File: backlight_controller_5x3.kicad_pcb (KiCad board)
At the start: 2 copper layers, 121.3 x 67.3 mm, 39 parts, among them J1 M12-5_RCPT_F, J2 M12-5_RCPT_F, J3 DB9F, J4 DB9M, P1 MINI_FIT_JR_02X03_M_RA, P2 PWR_JACK_2.5x5.5, U1 SN74ABT541BDWR, U2 SN74ABT541BDWR

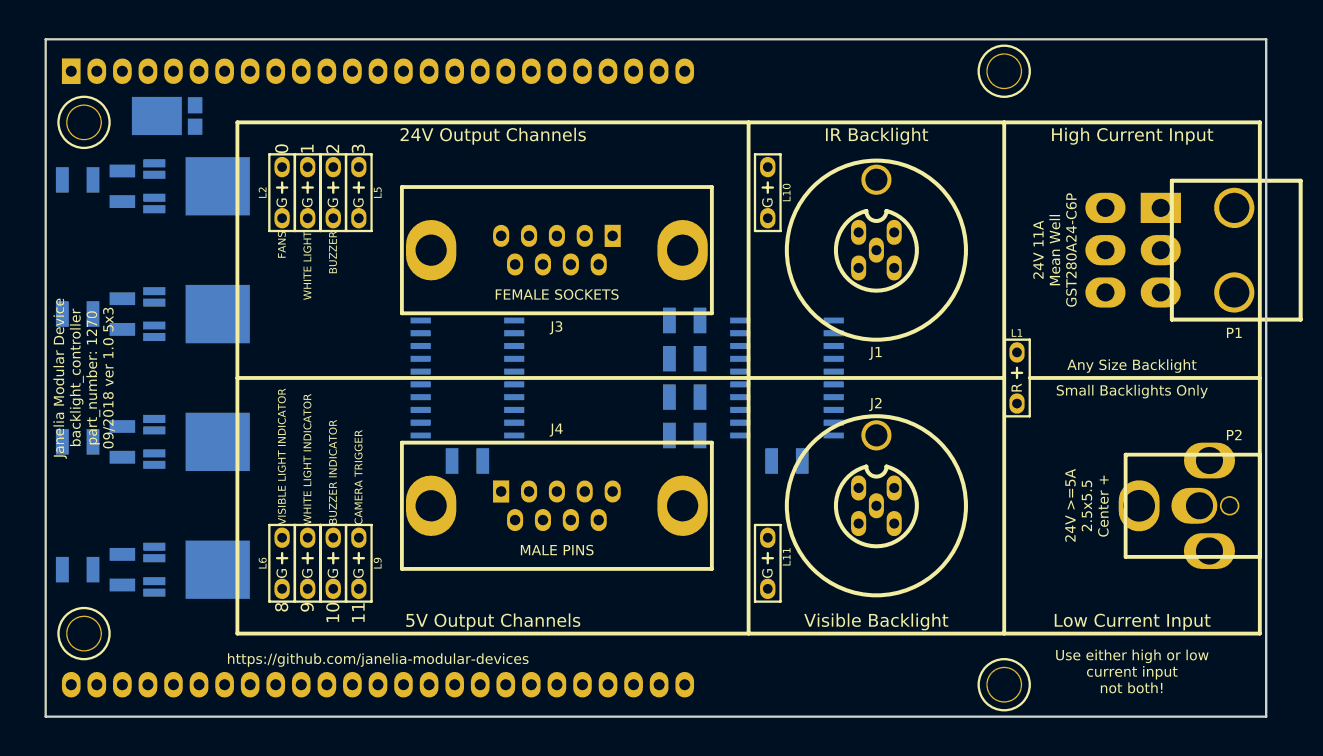
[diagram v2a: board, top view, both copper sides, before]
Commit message: Initial footprint layout.
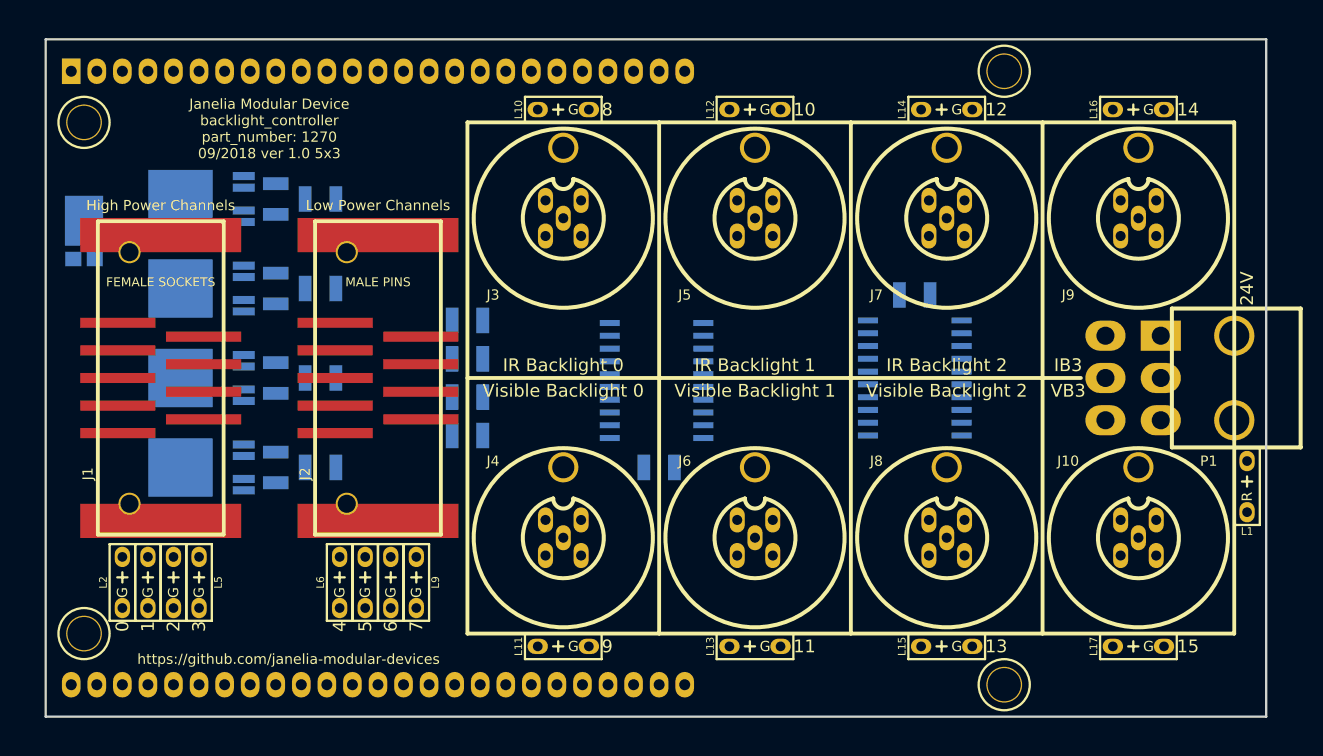
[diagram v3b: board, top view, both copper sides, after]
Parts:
- removed P2: PWR_JACK_2.5x5.5, backlight_controller_5x3:DCJACK_2PIN_HIGHCURRENT
- added J10: M12-5_RCPT_F, backlight_controller_5x3:M12-5_RCPT_F, F.Cu at (178.4, 121.3)
- added J5: M12-5_RCPT_F, backlight_controller_5x3:M12-5_RCPT_F, F.Cu at (140.3, 89.5)
- added J6: M12-5_RCPT_F, backlight_controller_5x3:M12-5_RCPT_F, F.Cu at (140.3, 121.3)
- added J7: M12-5_RCPT_F, backlight_controller_5x3:M12-5_RCPT_F, F.Cu at (159.4, 89.5)
- added J8: M12-5_RCPT_F, backlight_controller_5x3:M12-5_RCPT_F, F.Cu at (159.4, 121.3)
- added J9: M12-5_RCPT_F, backlight_controller_5x3:M12-5_RCPT_F, F.Cu at (178.4, 89.5)
- added L12: LED_5V_GRN, backlight_controller_5x3:LED_555-3XXX_G, F.Cu at (140.3, 78.7)
- added L13: LED_5V_GRN, backlight_controller_5x3:LED_555-3XXX_G, F.Cu at (140.3, 132.1)
- added L14: LED_5V_GRN, backlight_controller_5x3:LED_555-3XXX_G, F.Cu at (159.4, 78.7)
- added L15: LED_5V_GRN, backlight_controller_5x3:LED_555-3XXX_G, F.Cu at (159.4, 132.1)
- added L16: LED_5V_GRN, backlight_controller_5x3:LED_555-3XXX_G, F.Cu at (178.4, 78.7)
- added L17: LED_5V_GRN, backlight_controller_5x3:LED_555-3XXX_G, F.Cu at (178.4, 132.1)
- J1: value M12-5_RCPT_F -> DB9F_SMD; footprint backlight_controller_5x3:M12-5_RCPT_F -> footprints:DB9F_SMD
- J2: value M12-5_RCPT_F -> DB9M_SMD; footprint backlight_controller_5x3:M12-5_RCPT_F -> footprints:DB9M_SMD
- J3: value DB9F -> M12-5_RCPT_F; footprint backlight_controller_5x3:DB9F -> backlight_controller_5x3:M12-5_RCPT_F
- J4: value DB9M -> M12-5_RCPT_F; footprint backlight_controller_5x3:DB9M -> backlight_controller_5x3:M12-5_RCPT_F
- R5, R6, R7, R8: value 35.7 -> 140
- moved J1 72.2 mm to (81.3, 105.4), turned to 90 degrees
- moved J2 51.1 mm to (102.9, 105.4), turned to 90 degrees
- moved L2 41.9 mm to (77.5, 125.7)
- moved L3 41.9 mm to (80.0, 125.7)
- moved L4 41.9 mm to (82.5, 125.7)
- moved L5 41.9 mm to (85.1, 125.7)
- moved R4 26.2 mm to (97.2, 114.3), turned to 0 degrees
- moved L1 25.3 mm to (189.2, 116.2)
- moved R3 25.0 mm to (97.2, 105.4), turned to 0 degrees
- moved R2 24.3 mm to (97.2, 96.5), turned to 0 degrees
- moved R1 24.2 mm to (97.2, 87.6), turned to 0 degrees
- moved L10 21.9 mm to (121.3, 78.7), turned to 90 degrees
- moved L11 21.9 mm to (121.3, 132.1), turned to 90 degrees
- moved R5 21.6 mm to (111.8, 99.7)
- moved R6 21.6 mm to (111.8, 103.5)
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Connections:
- net /output_0/FAULT renamed /high_power_outputs/fans/FAULT
- net /output_1/FAULT renamed /high_power_outputs/white_light/FAULT
- net /output_2/FAULT renamed /high_power_outputs/buzzer/FAULT
- net /output_3/FAULT renamed /high_power_outputs/output_3/FAULT
- HPS1 pad 6: /FANS -> /high_power_outputs/OUTPUT_0
- HPS2 pad 6: /WHITE_LIGHT -> /high_power_outputs/OUTPUT_1
- HPS3 pad 6: /BUZZER -> /high_power_outputs/OUTPUT_2
- HPS4 pad 6: /OUTPUT_3 -> /high_power_outputs/OUTPUT_3
- J1 pad 2: (no net) -> /high_power_outputs/OUTPUT_0
- J1 pad 3: GND -> VAA
- J1 pad 4: /C_12 -> /high_power_outputs/OUTPUT_1
- J2 pad 1: VAA -> GND
- J2 pad 2: (no net) -> /low_power_outputs/OUTPUT_0
- J2 pad 4: /C_13 -> /low_power_outputs/OUTPUT_1
- J2 pad 5: VAA -> GND
- J3 pad 2: /FANS -> (no net)
- J3 pad 3: VAA -> GND
- J3 pad 4: /WHITE_LIGHT -> /C_8
- J4 pad 1: GND -> VAA
- J4 pad 2: /VISIBLE_LIGHT_INDICATOR -> (no net)
- J4 pad 4: /WHITE_LIGHT_INDICATOR -> /C_9
- J4 pad 5: GND -> VAA
- L10 pad 1: /C_12 -> /C_8
- L11 pad 1: /C_13 -> /C_9
- L6 pad 1: /C_8 -> /C_4
- L7 pad 1: /C_9 -> /C_5
- L8 pad 1: /C_10 -> /C_6
- L9 pad 1: /C_11 -> /C_7
- R5 pad 1: /VISIBLE_LIGHT_INDICATOR -> /low_power_outputs/OUTPUT_0
- R5 pad 2: /C_8 -> /C_4
- R6 pad 1: /WHITE_LIGHT_INDICATOR -> /low_power_outputs/OUTPUT_1
- R6 pad 2: /C_9 -> /C_5
- R7 pad 1: /BUZZER_INDICATOR -> /low_power_outputs/OUTPUT_2
- R7 pad 2: /C_10 -> /C_6
- R8 pad 1: /CAMERA_TRIGGER -> /low_power_outputs/OUTPUT_3
- R8 pad 2: /C_11 -> /C_7
- U1 pad 11: (no net) -> /C_7
- U1 pad 12: (no net) -> /C_6
- U1 pad 13: (no net) -> /C_5
- U1 pad 14: (no net) -> /C_4
- U2 pad 11: (no net) -> /C_15
- U2 pad 12: (no net) -> /C_14
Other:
- board text added: "12"
- board text added: "13"
- board text added: "14"
- board text added: "15"
- board text added: "24V"
- board text added: "4"
- board text added: "5"
- board text added: "6"
- board text added: "7"
- board text added: "High Power Channels"
- board text added: "IB3"
- board text added: "IR Backlight 0"
- board text added: "IR Backlight 1"
- board text added: "IR Backlight 2"
- board text added: "Low Power Channels"
- board text added: "VB3"
- board text added: "Visible Backlight 0"
- board text added: "Visible Backlight 1"
- board text added: "Visible Backlight 2"
- board text removed: "24V 11A Mean Well GST280A24-C6P"
- board text removed: "24V >=5A 2.5x5.5 Center +"
- board text removed: "24V Output Channels"
- board text removed: "5V Output Channels"
- board text removed: "Any Size Backlight"
- board text removed: "BUZZER"
- board text removed: "BUZZER INDICATOR"
- board text removed: "CAMERA TRIGGER"
- board text removed: "FANS"
- board text removed: "High Current Input"
- board text removed: "IR Backlight"
- board text removed: "Low Current Input"
- board text removed: "Small Backlights Only"
- board text removed: "Use either high or low current input not both!"
- board text removed: "VISIBLE LIGHT INDICATOR"
- board text removed: "Visible Backlight"
- board text removed: "WHITE LIGHT"
- board text removed: "WHITE LIGHT INDICATOR"

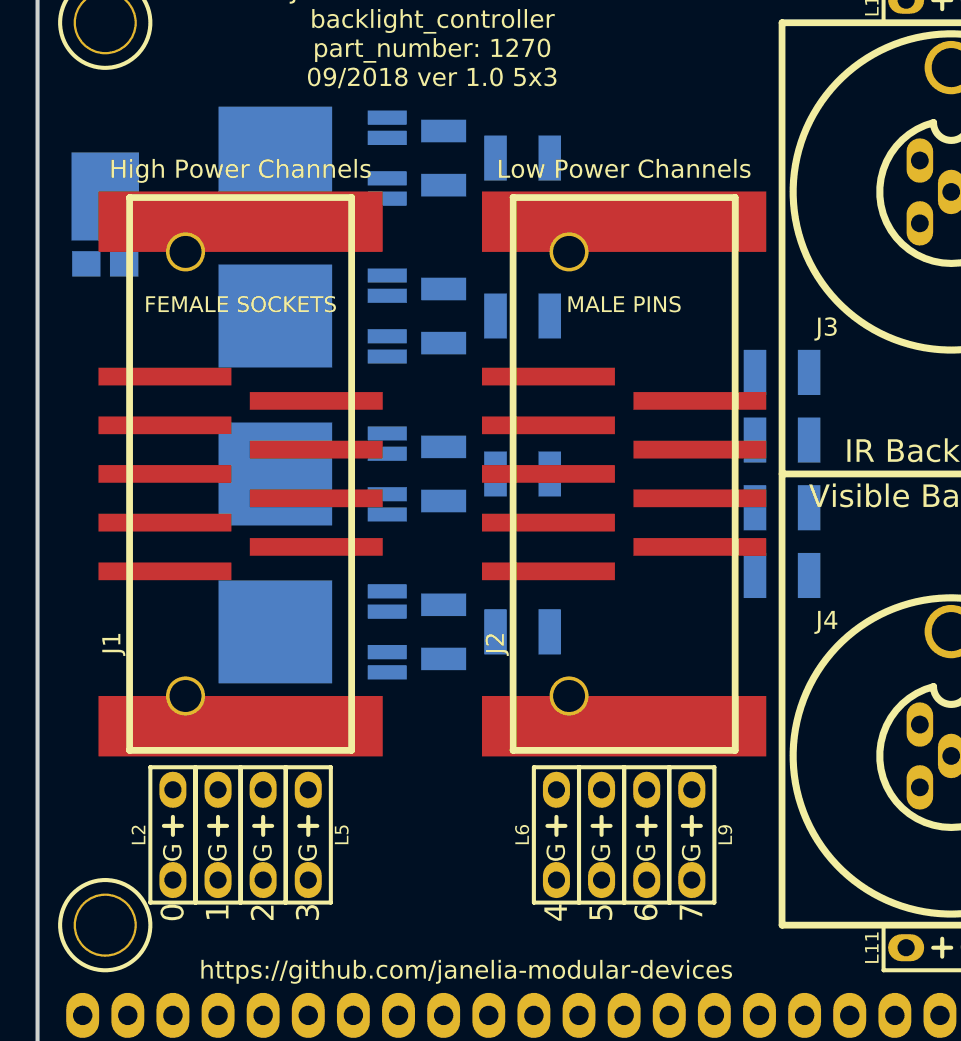
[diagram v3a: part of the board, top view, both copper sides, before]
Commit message: Another schematic reorganization.
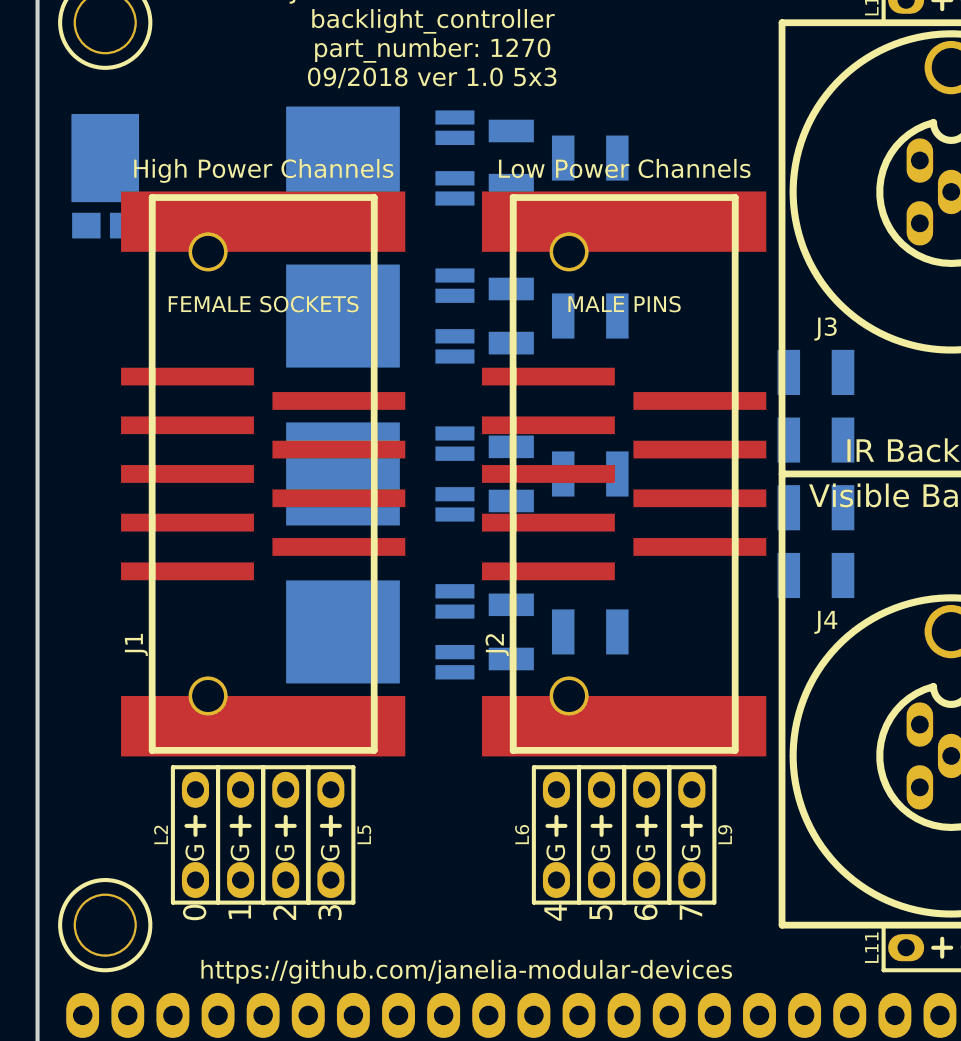
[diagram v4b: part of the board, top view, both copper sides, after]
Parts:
- moved C3 3.81 mm to (96.5, 87.6)
- moved C4 3.81 mm to (96.5, 96.5)
- moved C5 3.81 mm to (96.5, 105.4)
- moved C6 3.81 mm to (96.5, 114.3)
- moved HPS1 3.81 mm to (93.3, 87.6)
- moved HPS2 3.81 mm to (93.3, 96.5)
- moved HPS3 3.81 mm to (93.3, 105.4)
- moved HPS4 3.81 mm to (93.3, 114.3)
- moved R1 3.81 mm to (101.0, 87.6)
- moved R2 3.81 mm to (101.0, 96.5)
- moved R3 3.81 mm to (101.0, 105.4)
- moved R4 3.81 mm to (101.0, 114.3)
- moved D1 2.16 mm to (73.7, 88.7)
- moved R5 1.91 mm to (113.7, 99.7)
- moved R6 1.91 mm to (113.7, 103.5)
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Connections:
- net /high_power_outputs/buzzer/FAULT renamed /high_power_outputs/high_power_output_2/FAULT
- net /high_power_outputs/fans/FAULT renamed /high_power_outputs/high_power_output_0/FAULT
- net /high_power_outputs/output_3/FAULT renamed /high_power_outputs/high_power_output_3/FAULT
- net /high_power_outputs/white_light/FAULT renamed /high_power_outputs/high_power_output_1/FAULT

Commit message: Reorganized schematics, ready to layout traces.
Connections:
- net /C_0 renamed /backlight_5x3/C_0
- net /C_1 renamed /backlight_5x3/C_1
- net /C_10 renamed /backlight_5x3/C_10
- net /C_11 renamed /backlight_5x3/C_11
- net /C_12 renamed /backlight_5x3/C_12
- net /C_13 renamed /backlight_5x3/C_13
- net /C_14 renamed /backlight_5x3/C_14
- net /C_15 renamed /backlight_5x3/C_15
- net /C_2 renamed /backlight_5x3/C_2
- net /C_3 renamed /backlight_5x3/C_3
- net /C_4 renamed /backlight_5x3/C_4
- net /C_5 renamed /backlight_5x3/C_5
- net /C_6 renamed /backlight_5x3/C_6
- net /C_7 renamed /backlight_5x3/C_7
- net /C_8 renamed /backlight_5x3/C_8
- net /C_9 renamed /backlight_5x3/C_9
- net /high_power_outputs/OUTPUT_0 renamed /backlight_5x3/high_power_outputs/OUTPUT_0
- net /high_power_outputs/OUTPUT_1 renamed /backlight_5x3/high_power_outputs/OUTPUT_1
- net /high_power_outputs/OUTPUT_2 renamed /backlight_5x3/high_power_outputs/OUTPUT_2
- net /high_power_outputs/OUTPUT_3 renamed /backlight_5x3/high_power_outputs/OUTPUT_3
- net /high_power_outputs/high_power_output_0/FAULT renamed /backlight_5x3/high_power_outputs/high_power_output_0/FAULT
- net /high_power_outputs/high_power_output_1/FAULT renamed /backlight_5x3/high_power_outputs/high_power_output_1/FAULT
- net /high_power_outputs/high_power_output_2/FAULT renamed /backlight_5x3/high_power_outputs/high_power_output_2/FAULT
- net /high_power_outputs/high_power_output_3/FAULT renamed /backlight_5x3/high_power_outputs/high_power_output_3/FAULT
- net /low_power_outputs/OUTPUT_0 renamed /backlight_5x3/low_power_outputs/OUTPUT_0
- net /low_power_outputs/OUTPUT_1 renamed /backlight_5x3/low_power_outputs/OUTPUT_1
- net /low_power_outputs/OUTPUT_2 renamed /backlight_5x3/low_power_outputs/OUTPUT_2
- net /low_power_outputs/OUTPUT_3 renamed /backlight_5x3/low_power_outputs/OUTPUT_3

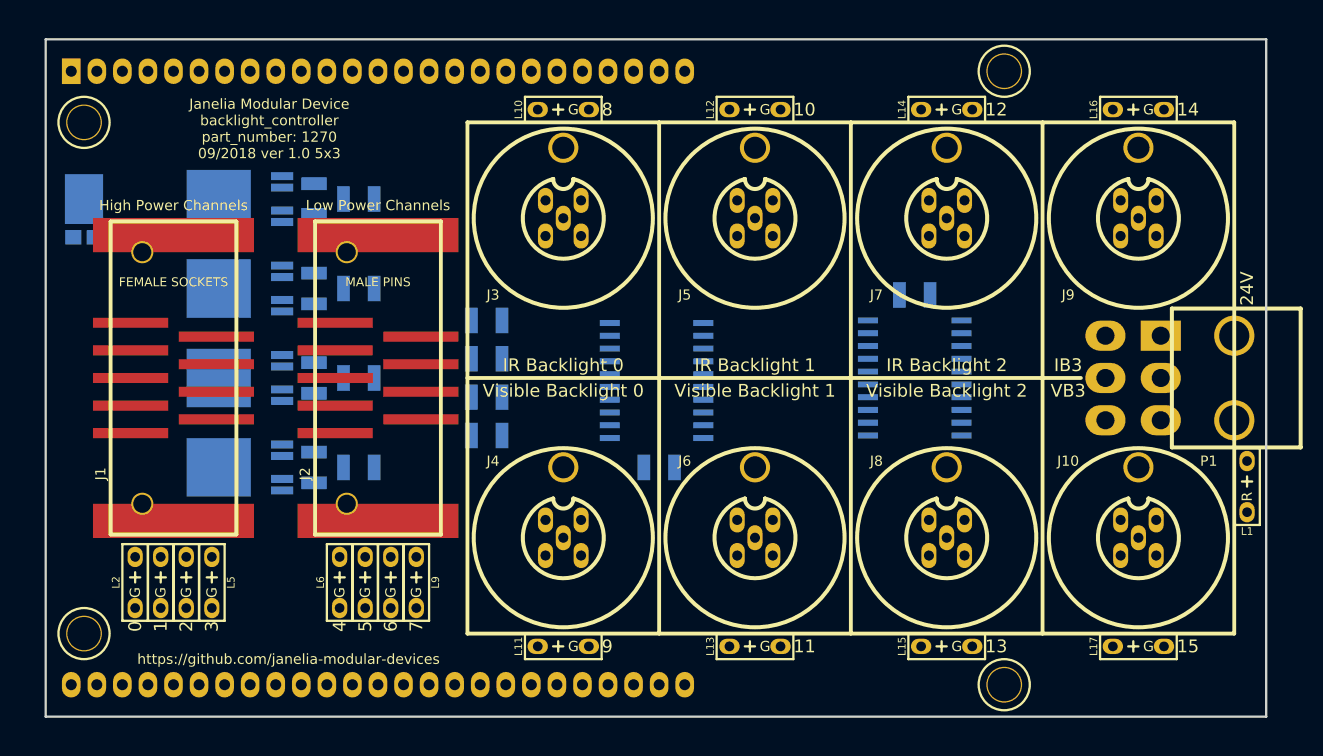
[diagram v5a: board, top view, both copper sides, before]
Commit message: Added autorouted traces.
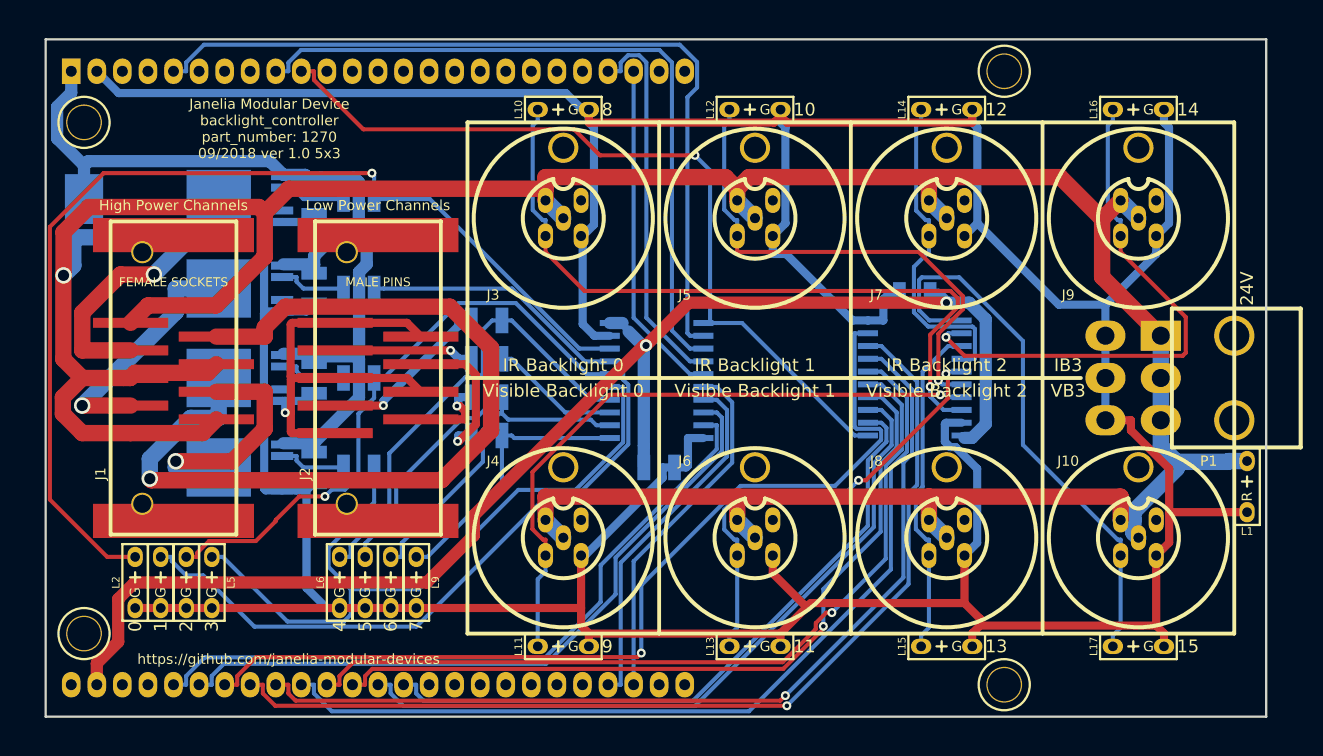
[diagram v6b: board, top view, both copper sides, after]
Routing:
- net GND: track 0.00 -> 517.9 mm, vias 0 -> 1
- net VAA: track 0.00 -> 322.4 mm, vias 0 -> 1
- net VEE: track 0.00 -> 141.9 mm, vias 0 -> 2
- net /backlight_5x3/C_0: track 0.00 -> 104.4 mm, vias 0 -> 1
- net /CHANNEL_14: track 0.00 -> 98.6 mm, vias 0 -> 1
- net VDD: track 0.00 -> 94.5 mm
- net /CHANNEL_15: track 0.00 -> 94.1 mm, vias 0 -> 1
- net /CHANNEL_13: track 0.00 -> 93.3 mm, vias 0 -> 1
- net /backlight_5x3/C_1: track 0.00 -> 93.3 mm
- net /backlight_5x3/high_power_outputs/OUTPUT_2: track 0.00 -> 89.5 mm, vias 0 -> 1
- net /CHANNEL_12: track 0.00 -> 88.7 mm
- net /CHANNEL_0: track 0.00 -> 83.4 mm
- net /CHANNEL_11: track 0.00 -> 81.7 mm, vias 0 -> 1
- net /~ENABLE: track 0.00 -> 81.4 mm, vias 0 -> 1
- net /CHANNEL_10: track 0.00 -> 77.6 mm, vias 0 -> 1
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
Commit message: Finished version 1.0.
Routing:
- net GND: track 517.9 -> 557.6 mm
- net VDD: track 94.5 -> 121.9 mm, vias 0 -> 2
- net /CHANNEL_8: track 67.1 -> 93.7 mm, vias 0 -> 1
- net /backlight_5x3/C_1: track 93.3 -> 68.3 mm
- net /backlight_5x3/C_0: track 104.4 -> 80.3 mm, vias 1 -> 0
- net /CHANNEL_14: track 98.6 -> 77.4 mm, vias 1 -> 2
- net /backlight_5x3/C_14: track 54.3 -> 34.1 mm, vias 1 -> 2
- net /CHANNEL_0: track 83.4 -> 64.1 mm, vias 0 -> 2
- net /CHANNEL_11: track 81.7 -> 100.1 mm
- net /CHANNEL_1: track 71.8 -> 54.6 mm, vias 0 -> 2
- net /backlight_5x3/high_power_outputs/OUTPUT_2: track 89.5 -> 73.2 mm
- net /CHANNEL_5: track 35.7 -> 50.4 mm, vias 0 -> 1
- net /CHANNEL_13: track 93.3 -> 79.0 mm, vias 1 -> 2
- net /CHANNEL_4: track 35.6 -> 49.7 mm, vias 0 -> 1
- net /backlight_5x3/C_13: track 33.5 -> 46.6 mm, vias 0 -> 1
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- added copper zone on B.Cu, net GND
- added copper zone on F.Cu, net VAA
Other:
- net class GND: trace_width 0.8128 -> 1.4224
